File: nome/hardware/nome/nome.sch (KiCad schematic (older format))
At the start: 48 parts, among them J1 Audio-Jack-3_2Switches, J2 Conn_02x05_Odd_Even, SW1 SW_SPST, SW2 Rotary_Encoder_Switch, U1 LM1117-1.8, U2 LM1117-3.3, U3 AS1115, U4 STMF411CEU6, U5 LTC-4727JS, U6 CS43L22

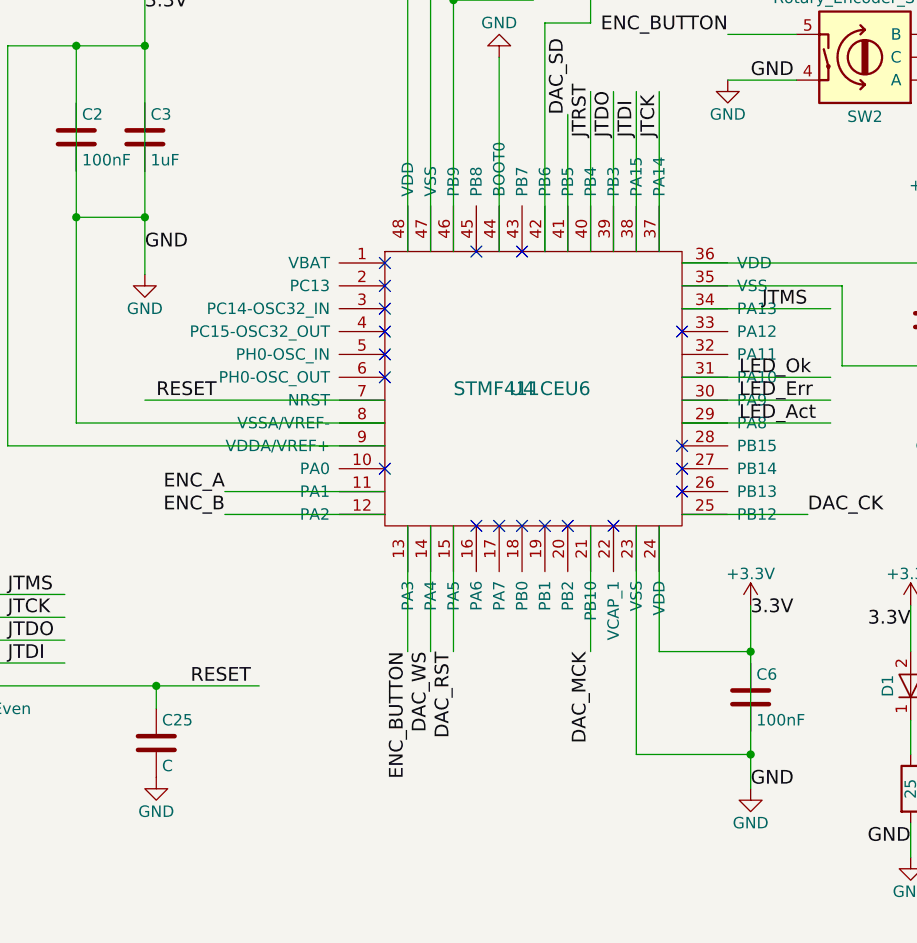
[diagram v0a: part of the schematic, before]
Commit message: Tie in VCAP and VBAT
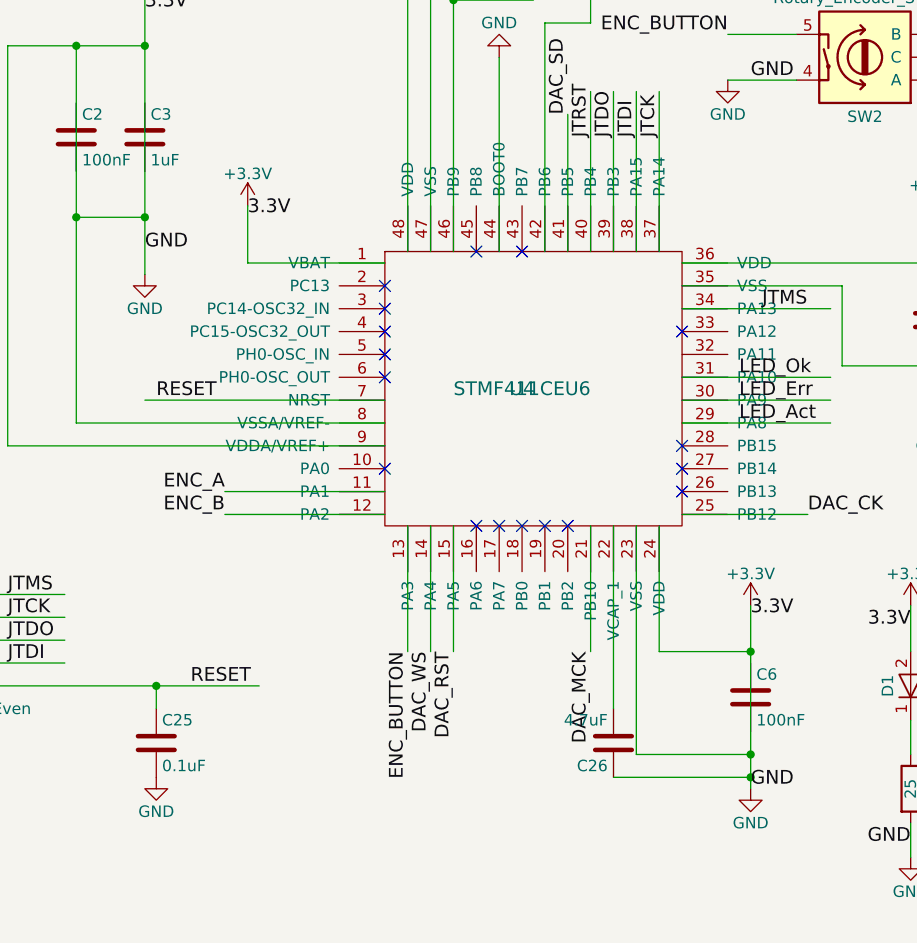
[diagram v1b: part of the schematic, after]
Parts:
- added C26: 4.7uF, symbol C
- C25: value C -> 0.1uF
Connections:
- wire segments 218 -> 222
- no-connect marks 41 -> 39
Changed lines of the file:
@@
 DAC_WS
 $Comp
-L GND #PWR19
+L GND #PWR20
 U 1 1 59E78773
 P 4850 6000
-F 0 "#PWR19" H 4850 5750 50  0001 C CNN
+F 0 "#PWR20" H 4850 5750 50  0001 C CNN
 F 1 "GND" H 4850 5850 50  0000 C CNN
 F 2 "" H 4850 6000 50  0001 C CNN
@@
 $EndComp
 $Comp
-L GND #PWR23
+L GND #PWR24
 U 1 1 59E789AE
 P 5650 4350
-F 0 "#PWR23" H 5650 4100 50  0001 C CNN
+F 0 "#PWR24" H 5650 4100 50  0001 C CNN
 F 1 "GND" H 5650 4200 50  0000 C CNN
 F 2 "" H 5650 4350 50  0001 C CNN
@@
 GND
 $Comp
-L GND #PWR16
+L GND #PWR17
 U 1 1 59E785A7
 P 4150 2050
-F 0 "#PWR16" H 4150 1800 50  0001 C CNN
+F 0 "#PWR17" H 4150 1800 50  0001 C CNN
 F 1 "GND" H 4150 1900 50  0000 C CNN
 F 2 "" H 4150 2050 50  0001 C CNN
@@
 ENC_BUTTON
 $Comp
-L GND #PWR17
+L GND #PWR18
 U 1 1 59E7A59F
 P 4750 2900
-F 0 "#PWR17" H 4750 2650 50  0001 C CNN
+F 0 "#PWR18" H 4750 2650 50  0001 C CNN
 F 1 "GND" H 4750 2750 50  0000 C CNN
 F 2 "" H 4750 2900 50  0001 C CNN
@@
 GND
 $Comp
-L GND #PWR27
+L GND #PWR28
 U 1 1 59E7A91F
 P 6200 2800
-F 0 "#PWR27" H 6200 2550 50  0001 C CNN
+F 0 "#PWR28" H 6200 2550 50  0001 C CNN
 F 1 "GND" H 6200 2650 50  0000 C CNN
 F 2 "" H 6200 2800 50  0001 C CNN
@@
 $EndComp
 $Comp
-L GND #PWR32
+L GND #PWR33
 U 1 1 59E7B33F
 P 6950 5050
-F 0 "#PWR32" H 6950 4800 50  0001 C CNN
+F 0 "#PWR33" H 6950 4800 50  0001 C CNN
 F 1 "GND" H 6950 4900 50  0000 C CNN
 F 2 "" H 6950 5050 50  0001 C CNN
@@
 $EndComp
 $Comp
-L GND #PWR37
+L GND #PWR38
 U 1 1 59E7B49E
 P 8900 1550
-F 0 "#PWR37" H 8900 1300 50  0001 C CNN
+F 0 "#PWR38" H 8900 1300 50  0001 C CNN
 F 1 "GND" H 8900 1400 50  0000 C CNN
 F 2 "" H 8900 1550 50  0001 C CNN
@@
 GND
 $Comp
-L GND #PWR39
+L GND #PWR40
 U 1 1 59E7B719
 P 9050 2500
-F 0 "#PWR39" H 9050 2250 50  0001 C CNN
+F 0 "#PWR40" H 9050 2250 50  0001 C CNN
 F 1 "GND" H 9050 2350 50  0000 C CNN
 F 2 "" H 9050 2500 50  0001 C CNN
@@
 $EndComp
 $Comp
-L GND #PWR41
+L GND #PWR42
 U 1 1 59E7BC76
 P 9950 3350
-F 0 "#PWR41" H 9950 3100 50  0001 C CNN
+F 0 "#PWR42" H 9950 3100 50  0001 C CNN
 F 1 "GND" H 9950 3200 50  0000 C CNN
 F 2 "" H 9950 3350 50  0001 C CNN
@@
 $EndComp
 $Comp
-L GND #PWR28
+L GND #PWR29
 U 1 1 59E7CFD0
 P 6300 4400
-F 0 "#PWR28" H 6300 4150 50  0001 C CNN
+F 0 "#PWR29" H 6300 4150 50  0001 C CNN
 F 1 "GND" H 6300 4250 50  0000 C CNN
 F 2 "" H 6300 4400 50  0001 C CNN
@@
 $EndComp
 $Comp
-L GND #PWR30
+L GND #PWR31
 U 1 1 59E7D220
 P 6700 3650
-F 0 "#PWR30" H 6700 3400 50  0001 C CNN
+F 0 "#PWR31" H 6700 3400 50  0001 C CNN
 F 1 "GND" H 6700 3500 50  0000 C CNN
 F 2 "" H 6700 3650 50  0001 C CNN
@@
 GND
 $Comp
-L GND #PWR31
+L GND #PWR32
 U 1 1 59E7D3C5
 P 6700 4600
-F 0 "#PWR31" H 6700 4350 50  0001 C CNN
+F 0 "#PWR32" H 6700 4350 50  0001 C CNN
 F 1 "GND" H 6700 4450 50  0000 C CNN
 F 2 "" H 6700 4600 50  0001 C CNN
@@
 GND
 $Comp
-L GND #PWR42
+L GND #PWR43
 U 1 1 59E82134
 P 10700 5800
-F 0 "#PWR42" H 10700 5550 50  0001 C CNN
+F 0 "#PWR43" H 10700 5550 50  0001 C CNN
 F 1 "GND" H 10700 5650 50  0000 C CNN
 F 2 "" H 10700 5800 50  0001 C CNN
@@
 $EndComp
 $Comp
-L GND #PWR35
+L GND #PWR36
 U 1 1 59E84953
 P 7500 6400
-F 0 "#PWR35" H 7500 6150 50  0001 C CNN
+F 0 "#PWR36" H 7500 6150 50  0001 C CNN
 F 1 "GND" H 7500 6250 50  0000 C CNN
 F 2 "" H 7500 6400 50  0001 C CNN
@@
 $EndComp
 $Comp
-L GND #PWR33
+L GND #PWR34
 U 1 1 59E96B30
 P 7050 2600
-F 0 "#PWR33" H 7050 2350 50  0001 C CNN
+F 0 "#PWR34" H 7050 2350 50  0001 C CNN
 F 1 "GND" H 7050 2450 50  0000 C CNN
 F 2 "" H 7050 2600 50  0001 C CNN
@@
 $EndComp
 $Comp
-L GND #PWR36
+L GND #PWR37
 U 1 1 59E9800C
 P 7550 2400
-F 0 "#PWR36" H 7550 2150 50  0001 C CNN
+F 0 "#PWR37" H 7550 2150 50  0001 C CNN
 F 1 "GND" H 7550 2250 50  0000 C CNN
 F 2 "" H 7550 2400 50  0001 C CNN
@@
 $EndComp
 $Comp
-L +1V8 #PWR12
+L +1V8 #PWR13
 U 1 1 59EBA3CB
 P 3150 700
-F 0 "#PWR12" H 3150 550 50  0001 C CNN
+F 0 "#PWR13" H 3150 550 50  0001 C CNN
 F 1 "+1V8" H 3150 840 50  0000 C CNN
 F 2 "" H 3150 700 50  0001 C CNN
@@
 1.8V
 $Comp
-L +1V8 #PWR25
+L +1V8 #PWR26
 U 1 1 59EBAC5C
 P 5950 3600
-F 0 "#PWR25" H 5950 3450 50  0001 C CNN
+F 0 "#PWR26" H 5950 3450 50  0001 C CNN
 F 1 "+1V8" H 5950 3740 50  0000 C CNN
 F 2 "" H 5950 3600 50  0001 C CNN
@@
 1.8V
 $Comp
-L +1V8 #PWR38
+L +1V8 #PWR39
 U 1 1 59EBB07D
 P 9050 1900
-F 0 "#PWR38" H 9050 1750 50  0001 C CNN
+F 0 "#PWR39" H 9050 1750 50  0001 C CNN
 F 1 "+1V8" H 9050 2040 50  0000 C CNN
 F 2 "" H 9050 1900 50  0001 C CNN
@@
 1.8V
 $Comp
-L +1V8 #PWR40
+L +1V8 #PWR41
 U 1 1 59EBB271
 P 9950 2500
-F 0 "#PWR40" H 9950 2350 50  0001 C CNN
+F 0 "#PWR41" H 9950 2350 50  0001 C CNN
 F 1 "+1V8" H 9950 2640 50  0000 C CNN
 F 2 "" H 9950 2500 50  0001 C CNN
@@
 1.8V
 $Comp
-L +1V8 #PWR34
+L +1V8 #PWR35
 U 1 1 59EBB434
 P 7500 5700
-F 0 "#PWR34" H 7500 5550 50  0001 C CNN
+F 0 "#PWR35" H 7500 5550 50  0001 C CNN
 F 1 "+1V8" H 7500 5840 50  0000 C CNN
 F 2 "" H 7500 5700 50  0001 C CNN
@@
 1.8V
 $Comp
-L +3.3V #PWR15
+L +3.3V #PWR16
 U 1 1 59EBC448
 P 4150 1200
-F 0 "#PWR15" H 4150 1050 50  0001 C CNN
+F 0 "#PWR16" H 4150 1050 50  0001 C CNN
 F 1 "+3.3V" H 4150 1340 50  0000 C CNN
 F 2 "" H 4150 1200 50  0001 C CNN
@@
 3.3V
 $Comp
-L +3.3V #PWR22
+L +3.3V #PWR23
 U 1 1 59EBC6B7
 P 5650 3500
-F 0 "#PWR22" H 5650 3350 50  0001 C CNN
+F 0 "#PWR23" H 5650 3350 50  0001 C CNN
 F 1 "+3.3V" H 5650 3640 50  0000 C CNN
 F 2 "" H 5650 3500 50  0001 C CNN
@@
 3.3V
 $Comp
-L +3.3V #PWR18
+L +3.3V #PWR19
 U 1 1 59EBC777
 P 4850 5200
-F 0 "#PWR18" H 4850 5050 50  0001 C CNN
+F 0 "#PWR19" H 4850 5050 50  0001 C CNN
 F 1 "+3.3V" H 4850 5340 50  0000 C CNN
 F 2 "" H 4850 5200 50  0001 C CNN
@@
 GND
 $Comp
-L +3.3V #PWR11
+L +3.3V #PWR12
 U 1 1 59EBE08C
 P 3050 1550
-F 0 "#PWR11" H 3050 1400 50  0001 C CNN
+F 0 "#PWR12" H 3050 1400 50  0001 C CNN
 F 1 "+3.3V" H 3050 1690 50  0000 C CNN
 F 2 "" H 3050 1550 50  0001 C CNN
@@
 NoConn ~ 8100 8650
 $Comp
-L GND #PWR13
+L GND #PWR14
 U 1 1 59EC6122
 P 3550 9200
-F 0 "#PWR13" H 3550 8950 50  0001 C CNN
+F 0 "#PWR14" H 3550 8950 50  0001 C CNN
 F 1 "GND" H 3550 9050 50  0000 C CNN
 F 2 "" H 3550 9200 50  0001 C CNN
@@
 $EndComp
 $Comp
-L GND #PWR21
+L GND #PWR22
 U 1 1 59ECDC25
 P 5550 6300
-F 0 "#PWR21" H 5550 6050 50  0001 C CNN
+F 0 "#PWR22" H 5550 6050 50  0001 C CNN
 F 1 "GND" H 5550 6150 50  0000 C CNN
 F 2 "" H 5550 6300 50  0001 C CNN
@@
 GND
 $Comp
-L GND #PWR24
+L GND #PWR25
 U 1 1 59ECDE0F
 P 5850 6300
-F 0 "#PWR24" H 5850 6050 50  0001 C CNN
+F 0 "#PWR25" H 5850 6050 50  0001 C CNN
 F 1 "GND" H 5850 6150 50  0000 C CNN
 F 2 "" H 5850 6300 50  0001 C CNN
@@
 $EndComp
 $Comp
-L GND #PWR26
+L GND #PWR27
 U 1 1 59ECDE7F
 P 6150 6300
-F 0 "#PWR26" H 6150 6050 50  0001 C CNN
+F 0 "#PWR27" H 6150 6050 50  0001 C CNN
 F 1 "GND" H 6150 6150 50  0000 C CNN
 F 2 "" H 6150 6300 50  0001 C CNN
@@
 $EndComp
 $Comp
-L GND #PWR29
+L GND #PWR30
 U 1 1 59ECE00C
 P 6450 6300
-F 0 "#PWR29" H 6450 6050 50  0001 C CNN
+F 0 "#PWR30" H 6450 6050 50  0001 C CNN
 F 1 "GND" H 6450 6150 50  0000 C CNN
 F 2 "" H 6450 6300 50  0001 C CNN
@@
 Text Label 7350 3600 0    60   ~ 0
 DAC_SCL
-NoConn ~ 3250 3700
 NoConn ~ 3250 3800
 NoConn ~ 3250 3900
@@
 NoConn ~ 3950 4850
 NoConn ~ 4050 4850
-NoConn ~ 4250 4850
 NoConn ~ 4550 4700
 NoConn ~ 4550 4600
@@
 	3750 3650 3750 2800
 $Comp
-L GND #PWR14
+L GND #PWR15
 U 1 1 59ED71C5
 P 3750 2800
-F 0 "#PWR14" H 3750 2550 50  0001 C CNN
+F 0 "#PWR15" H 3750 2550 50  0001 C CNN
 F 1 "GND" H 3750 2650 50  0000 C CNN
 F 2 "" H 3750 2800 50  0001 C CNN
@@
 JTRST
 $Comp
-L +3.3V #PWR20
+L +3.3V #PWR21
 U 1 1 59EDA31D
 P 5550 5200
-F 0 "#PWR20" H 5550 5050 50  0001 C CNN
+F 0 "#PWR21" H 5550 5050 50  0001 C CNN
 F 1 "+3.3V" H 5550 5340 50  0000 C CNN
 F 2 "" H 5550 5200 50  0001 C CNN
@@
 P 2250 5800
 F 0 "C25" H 2275 5900 50  0000 L CNN
-F 1 "C" H 2275 5700 50  0000 L CNN
+F 1 "0.1uF" H 2275 5700 50  0000 L CNN
 F 2 "" H 2288 5650 50  0001 C CNN
 F 3 "" H 2250 5800 50  0001 C CNN
@@
 Text Label 2250 4300 0    60   ~ 0
 RESET
+Wire Wire Line
+	4250 5950 4850 5950
+Connection ~ 4850 5950
+$Comp
+L C C26
+U 1 1 59EDD613
+P 4250 5800
+F 0 "C26" H 4275 5900 50  0000 L CNN
+F 1 "4.7uF" H 4275 5700 50  0000 L CNN
+F 2 "" H 4288 5650 50  0001 C CNN
+F 3 "" H 4250 5800 50  0001 C CNN
+	1    4250 5800
+	-1   0    0    1
+$EndComp
+Wire Wire Line
+	4250 4850 4250 5650
+Wire Wire Line
+	3250 3700 2650 3700
+Wire Wire Line
+	2650 3700 2650 3450
+$Comp
+L +3.3V #PWR11
+U 1 1 59EDDD84
+P 2650 3450
+F 0 "#PWR11" H 2650 3300 50  0001 C CNN
+F 1 "+3.3V" H 2650 3590 50  0000 C CNN
+F 2 "" H 2650 3450 50  0001 C CNN
+F 3 "" H 2650 3450 50  0001 C CNN
+	1    2650 3450
+	1    0    0    -1
+$EndComp
+Text Label 2650 3500 0    60   ~ 0
+3.3V
 $EndSCHEMATC

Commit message: Organize schematic by function
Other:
- note added: "Audio"
- note added: "JTAG / SWD"
- note added: "Microcontroller"
- note added: "Power"
- note added: "Status LED"
- note added: "User Interface"
- moved on the sheet: BT1, C10, C11, C12, C13, C14, C15, C16, C17, C18, C19, C2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

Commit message: Add DC barrel jack
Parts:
- added J3: Barrel_Jack, symbol Barrel_Jack
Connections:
- net labels removed: VCC
- wire segments 222 -> 224
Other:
- moved on the sheet: BT1

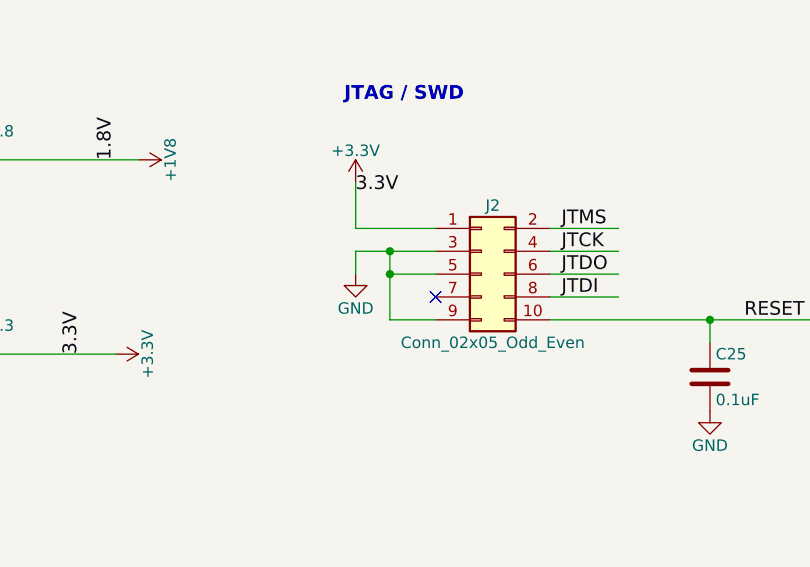
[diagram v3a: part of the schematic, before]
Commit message: Tie JTAG connector to GND in parallel
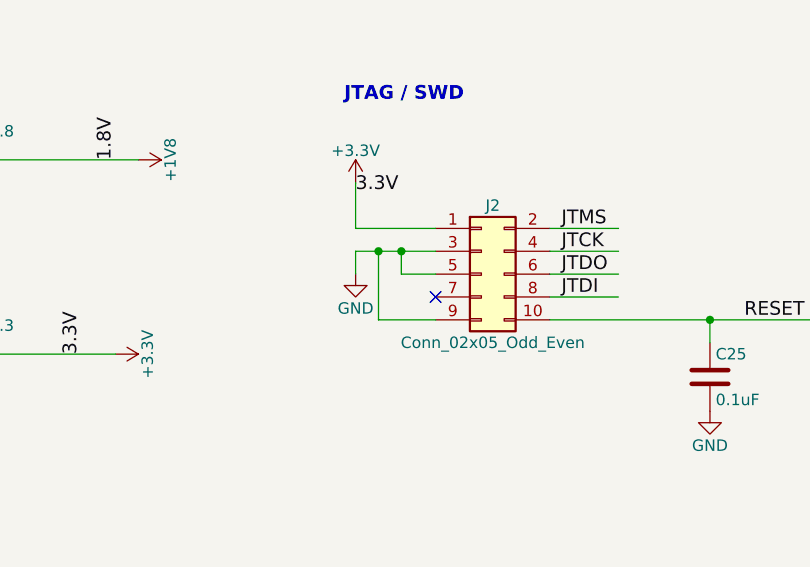
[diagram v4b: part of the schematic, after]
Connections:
- wire segments 224 -> 225
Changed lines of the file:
@@
 	5250 11450 6400 11450
-Wire Wire Line
-	4750 11250 4550 11250
-Wire Wire Line
-	4550 11150 4550 11450
 Wire Wire Line
 	4400 11150 4750 11150
 Wire Wire Line
 	4400 11150 4400 11250
-Connection ~ 4550 11150
-Wire Wire Line
-	4550 11450 4750 11450
-Connection ~ 4550 11250
 Wire Wire Line
 	4750 11050 4400 11050
@@
 	1450 11450 1450 10750
 Connection ~ 1450 10750
+Wire Wire Line
+	4750 11250 4600 11250
+Wire Wire Line
+	4600 11250 4600 11150
+Connection ~ 4600 11150
+Wire Wire Line
+	4750 11450 4500 11450
+Wire Wire Line
+	4500 11450 4500 11150
+Connection ~ 4500 11150
 $EndSCHEMATC

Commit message: Add a few simple footprints
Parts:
- D1, D2, D3, D4: footprint (none) -> LEDs:LED_0805_HandSoldering
- J2: footprint (none) -> Pin_Headers:Pin_Header_Straight_2x10_Pitch2.54mm

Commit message: Assign large chip footprints
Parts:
- U3: footprint (none) -> Housings_SSOP:QSOP-24_3.9x8.7mm_Pitch0.635mm
- U4: footprint (none) -> Housings_QFP:LQFP-48_7x7mm_Pitch0.5mm
- U6: footprint (none) -> Housings_DFN_QFN:QFN-40-1EP_6x6mm_Pitch0.5mm
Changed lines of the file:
@@
 F 0 "U6" H 9150 3100 60  0000 C CNN
 F 1 "CS43L22" H 9850 3700 60  0000 C CNN
-F 2 "" H 9900 3650 60  0001 C CNN
+F 2 "Housings_DFN_QFN:QFN-40-1EP_6x6mm_Pitch0.5mm" H 9900 3650 60  0001 C CNN
 F 3 "" H 9900 3650 60  0001 C CNN
 	1    9850 3700
@@
 F 0 "U4" H 3700 4150 60  0000 C CNN
 F 1 "STMF411CEU6" H 3700 4150 60  0000 C CNN
-F 2 "" H 3700 4150 60  0001 C CNN
+F 2 "Housings_QFP:LQFP-48_7x7mm_Pitch0.5mm" H 3700 4150 60  0001 C CNN
 F 3 "" H 3700 4150 60  0001 C CNN
 	1    3750 4150
@@
 F 0 "U3" H 3550 7450 60  0000 C CNN
 F 1 "AS1115" H 3550 7300 60  0000 C CNN
-F 2 "" H 3550 7300 60  0001 C CNN
+F 2 "Housings_SSOP:QSOP-24_3.9x8.7mm_Pitch0.635mm" H 3550 7300 60  0001 C CNN
 F 3 "" H 3550 7300 60  0001 C CNN
 	1    3600 7300
